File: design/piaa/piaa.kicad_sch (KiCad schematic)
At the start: 92 parts, among them J1 Screw_Terminal_01x03, J2 Conn_02x04_Counter_Clockwise, J3 Conn_02x01, J4 Conn_02x01, J5 Conn_02x01, J6 Screw_Terminal_01x06, J7 Screw_Terminal_01x05, P1 PS2805-4, Q1 FQT13N06L, Q2 FQT13N06L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

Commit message: fix symbols, begin layout
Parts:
- U8: footprint RPi_Pico:RPi_Pico_SMD_TH -> MCU_RaspberryPi_and_Boards:RPi_Pico_SMD_TH
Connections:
- net DIN2: now also P1.12 (C2); no longer P1.C2 (12)
- net DOUT4: no longer U4.3 (IN)
- net DOUT5: now also U4.3 (IN)
- net GND: now also Q1.3 (S), Q2.3 (S), Q3.3 (S), Q4.3 (S), Q5.3 (S), Q6.3 (S); no longer Q1.2 (S), Q2.2 (S), Q3.2 (S), Q4.2 (S), Q5.2 (S), Q6.2 (S)
- net at F3.2: now also Q3.4 (D); no longer Q3.3 (D)
- net at F2.2: now also Q2.4 (D); no longer Q2.3 (D)
- net at F1.2: now also Q1.4 (D); no longer Q1.3 (D)
- net at F6.2: now also Q6.4 (D); no longer Q6.3 (D)
- net at F4.2: now also Q4.4 (D); no longer Q4.3 (D)
- net at F5.2: now also Q5.4 (D); no longer Q5.3 (D)
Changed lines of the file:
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@@
     (effects (font (size 1.27 1.27)) (justify right))
   )
-  (hierarchical_label "DOUT4" (shape input) (at 25.4 180.34 180)
+  (hierarchical_label "DOUT5" (shape input) (at 25.4 180.34 180)
     (effects (font (size 1.27 1.27)) (justify right))
   )
@@
     (pin "2")
   )
-  (symbol (lib_id "piaalib:FQT13N06L") (at 58.42 121.92 0) (unit 1)
+  (symbol (lib_name "FQT13N06L_5") (lib_id "piaalib:FQT13N06L") (at 58.42 121.92 0) (unit 1)
     (in_bom yes) (on_board yes) (fields_autoplaced)
     (property "Reference" "Q2" (id 0) (at 64.77 120.6499 0)
@@
     (pin "2")
     (pin "3")
+    (pin "4")
   )
   (symbol (lib_id "power:GND") (at 63.5 191.77 0) (unit 1)
@@
     (pin "2")
     (pin "3")
+    (pin "4")
   )
   (symbol (lib_id "power:+5V") (at 151.13 104.14 0) (unit 1)
@@
     (property "Reference" "U8" (id 0) (at 147.32 13.97 0))
     (property "Value" "Pico" (id 1) (at 147.32 16.51 0))
-    (property "Footprint" "RPi_Pico:RPi_Pico_SMD_TH" (id 2) (at 147.32 45.72 90))
+    (property "Footprint" "MCU_RaspberryPi_and_Boards:RPi_Pico_SMD_TH" (id 2) (at 147.32 45.72 90))
     (property "Datasheet" "" (id 3) (at 147.32 45.72 0)
       (effects (font (size 1.27 1.27)) hide)
@@
     (pin "5")
   )
-  (symbol (lib_name "PTS12066V100_4") (lib_id "piaalib:PTS12066V100") (at 71.12 55.626 270) (unit 1)
+  (symbol (lib_id "piaalib:PTS12066V100") (at 71.12 55.626 270) (unit 1)
     (in_bom yes) (on_board yes)
     (property "Reference" "F6" (id 0) (at 66.04 58.42 90))
@@
     (pin "1")
   )
-  (symbol (lib_id "piaalib:FQT13N06L") (at 59.69 63.5 0) (unit 1)
+  (symbol (lib_name "FQT13N06L_3") (lib_id "piaalib:FQT13N06L") (at 59.69 63.5 0) (unit 1)
     (in_bom yes) (on_board yes) (fields_autoplaced)
     (property "Reference" "Q6" (id 0) (at 66.04 62.2299 0)
@@
     (pin "2")
     (pin "3")
+    (pin "4")
   )
   (symbol (lib_id "power:+5V") (at 21.59 166.37 0) (unit 1)
@@
     (pin "3")
   )
-  (symbol (lib_id "piaalib:FQT13N06L") (at 58.42 179.07 0) (unit 1)
+  (symbol (lib_name "FQT13N06L_4") (lib_id "piaalib:FQT13N06L") (at 58.42 179.07 0) (unit 1)
     (in_bom yes) (on_board yes) (fields_autoplaced)
     (property "Reference" "Q4" (id 0) (at 64.77 177.7999 0)
@@
     (pin "2")
     (pin "3")
+    (pin "4")
   )
   (symbol (lib_id "power:GND") (at 16.51 87.63 0) (unit 1)
@@
     (pin "2")
   )
-  (symbol (lib_name "PTS12066V100_3") (lib_id "piaalib:PTS12066V100") (at 71.12 25.146 270) (unit 1)
+  (symbol (lib_id "piaalib:PTS12066V100") (at 71.12 25.146 270) (unit 1)
     (in_bom yes) (on_board yes)
     (property "Reference" "F5" (id 0) (at 66.04 27.94 90))
@@
     (pin "2")
   )
-  (symbol (lib_name "PSD12C_1") (lib_id "piaalib:PSD12C") (at 175.26 142.24 270) (unit 1)
+  (symbol (lib_id "piaalib:PSD12C") (at 175.26 142.24 270) (unit 1)
     (in_bom yes) (on_board yes) (fields_autoplaced)
     (property "Reference" "D9" (id 0) (at 173.99 140.9699 90)
@@
     (pin "2")
   )
-  (symbol (lib_name "PTS12066V100_1") (lib_id "piaalib:PTS12066V100") (at 69.85 84.836 270) (unit 1)
+  (symbol (lib_id "piaalib:PTS12066V100") (at 69.85 84.836 270) (unit 1)
     (in_bom yes) (on_board yes)
     (property "Reference" "F1" (id 0) (at 64.77 87.63 90))
@@
     (pin "1")
   )
-  (symbol (lib_id "piaalib:FQT13N06L") (at 59.69 33.02 0) (unit 1)
+  (symbol (lib_name "FQT13N06L_2") (lib_id "piaalib:FQT13N06L") (at 59.69 33.02 0) (unit 1)
     (in_bom yes) (on_board yes) (fields_autoplaced)
     (property "Reference" "Q5" (id 0) (at 66.04 31.7499 0)
@@
     (pin "2")
     (pin "3")
+    (pin "4")
   )
   (symbol (lib_id "power:GND") (at 36.83 100.33 0) (unit 1)
@@
     (pin "10")
     (pin "11")
+    (pin "12")
     (pin "13")
     (pin "14")
@@
     (pin "8")
     (pin "9")
-    (pin "C2")
   )
   (symbol (lib_id "Device:R") (at 255.27 22.86 90) (unit 1)
@@
     (pin "2")
   )
-  (symbol (lib_id "piaalib:FQT13N06L") (at 58.42 149.86 0) (unit 1)
+  (symbol (lib_name "FQT13N06L_1") (lib_id "piaalib:FQT13N06L") (at 58.42 149.86 0) (unit 1)
     (in_bom yes) (on_board yes) (fields_autoplaced)
     (property "Reference" "Q3" (id 0) (at 64.77 148.5899 0)
@@
     (pin "2")
     (pin "3")
+    (pin "4")
   )
   (symbol (lib_id "power:GND") (at 16.51 175.26 0) (unit 1)
@@
     (pin "1")
   )
-  (symbol (lib_name "USMF020_1") (lib_id "piaalib:USMF020") (at 180.34 110.49 0) (unit 1)
+  (symbol (lib_id "piaalib:USMF020") (at 180.34 110.49 0) (unit 1)
     (in_bom yes) (on_board yes)
     (property "Reference" "PS1" (id 0) (at 181.61 111.76 0))
@@
     (pin "2")
   )
-  (symbol (lib_name "PTS12066V100_2") (lib_id "piaalib:PTS12066V100") (at 69.85 172.466 270) (unit 1)
+  (symbol (lib_id "piaalib:PTS12066V100") (at 69.85 172.466 270) (unit 1)
     (in_bom yes) (on_board yes)
     (property "Reference" "F4" (id 0) (at 64.77 175.26 90))
@@
     (pin "1")
   )
-  (symbol (lib_name "PTS12066V100_5") (lib_id "piaalib:PTS12066V100") (at 69.85 114.046 270) (unit 1)
+  (symbol (lib_id "piaalib:PTS12066V100") (at 69.85 114.046 270) (unit 1)
     (in_bom yes) (on_board yes)
     (property "Reference" "F2" (id 0) (at 64.77 116.84 90))
@@
     (pin "2")
   )
-  (symbol (lib_name "PSD12C_2") (lib_id "piaalib:PSD12C") (at 175.26 123.19 270) (unit 1)
+  (symbol (lib_id "piaalib:PSD12C") (at 175.26 123.19 270) (unit 1)
     (in_bom yes) (on_board yes)
     (property "Reference" "D8" (id 0) (at 173.99 120.65 90)
@@
     )
     (path "/28ea4dcd-d9fa-4361-9269-bd436148a234"
-      (reference "U8") (unit 1) (value "Pico") (footprint "RPi_Pico:RPi_Pico_SMD_TH")
+      (reference "U8") (unit 1) (value "Pico") (footprint "MCU_RaspberryPi_and_Boards:RPi_Pico_SMD_TH")
     )
     (path "/19057f4d-07e4-4313-ba58-58576df1fe00/c116edb4-51d5-471f-97e9-f783ce1a4554"

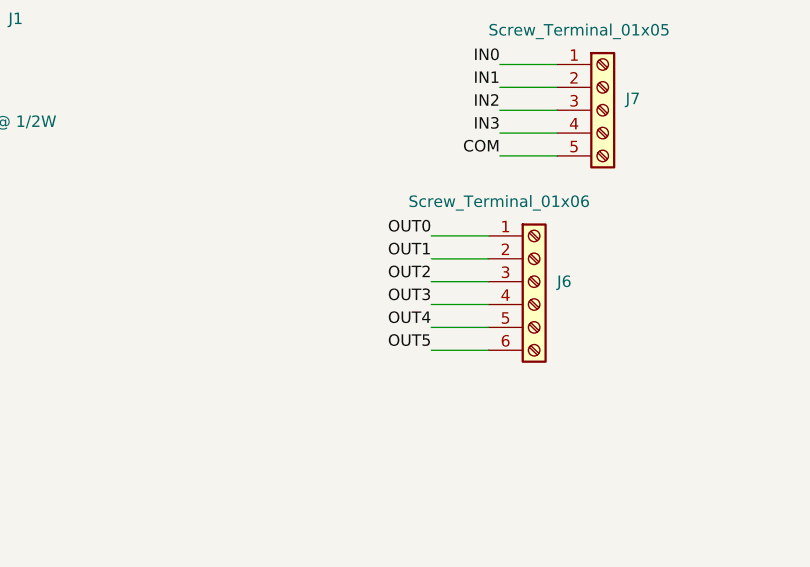
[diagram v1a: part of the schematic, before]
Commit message: update to pcb drawing
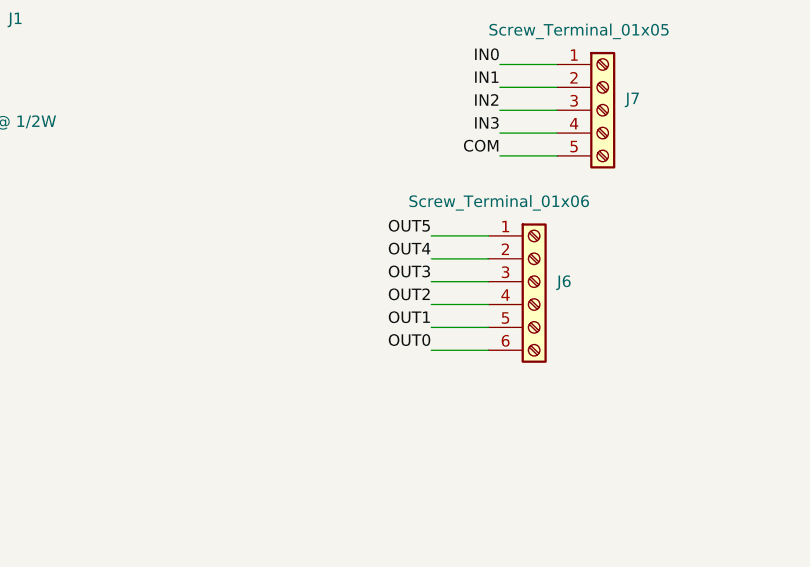
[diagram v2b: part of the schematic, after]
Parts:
- J7: footprint Connector_PinHeader_2.00mm:PinHeader_1x05_P2.00mm_Horizontal -> Connector_PinHeader_2.00mm:PinHeader_1x05_P2.00mm_Vertical
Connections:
- net OUT0: now also J6.6 (Pin_6); no longer J6.1 (Pin_1)
- net OUT1: now also J6.5 (Pin_5); no longer J6.2 (Pin_2)
- net OUT2: now also J6.4 (Pin_4); no longer J6.3 (Pin_3)
- net OUT3: now also J6.3 (Pin_3); no longer J6.4 (Pin_4)
- net OUT4: now also J6.2 (Pin_2); no longer J6.5 (Pin_5)
- net OUT5: now also J6.1 (Pin_1); no longer J6.6 (Pin_6)
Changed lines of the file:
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@@
     (effects (font (size 1.27 1.27)) (justify left bottom))
   )
-  (label "OUT5" (at 255.27 156.21 180)
+  (label "OUT0" (at 255.27 156.21 180)
     (effects (font (size 1.27 1.27)) (justify right bottom))
   )
@@
     (effects (font (size 1.27 1.27)) (justify left bottom))
   )
-  (label "OUT2" (at 255.27 148.59 180)
+  (label "OUT3" (at 255.27 148.59 180)
     (effects (font (size 1.27 1.27)) (justify right bottom))
   )
@@
     (effects (font (size 1.27 1.27)) (justify left bottom))
   )
-  (label "OUT1" (at 255.27 146.05 180)
+  (label "OUT4" (at 255.27 146.05 180)
     (effects (font (size 1.27 1.27)) (justify right bottom))
   )
@@
     (effects (font (size 1.27 1.27)) (justify left bottom))
   )
-  (label "OUT3" (at 255.27 151.13 180)
+  (label "OUT2" (at 255.27 151.13 180)
     (effects (font (size 1.27 1.27)) (justify right bottom))
   )
-  (label "OUT4" (at 255.27 153.67 180)
+  (label "OUT1" (at 255.27 153.67 180)
     (effects (font (size 1.27 1.27)) (justify right bottom))
   )
@@
     (effects (font (size 1.27 1.27)) (justify left bottom))
   )
-  (label "OUT0" (at 255.27 143.51 180)
+  (label "OUT5" (at 255.27 143.51 180)
     (effects (font (size 1.27 1.27)) (justify right bottom))
   )
@@
     (pin "2")
   )
-  (symbol (lib_name "FQT13N06L_5") (lib_id "piaalib:FQT13N06L") (at 58.42 121.92 0) (unit 1)
+  (symbol (lib_id "piaalib:FQT13N06L") (at 58.42 121.92 0) (unit 1)
     (in_bom yes) (on_board yes) (fields_autoplaced)
     (property "Reference" "Q2" (id 0) (at 64.77 120.6499 0)
@@
     (pin "1")
   )
-  (symbol (lib_name "FQT13N06L_3") (lib_id "piaalib:FQT13N06L") (at 59.69 63.5 0) (unit 1)
+  (symbol (lib_id "piaalib:FQT13N06L") (at 59.69 63.5 0) (unit 1)
     (in_bom yes) (on_board yes) (fields_autoplaced)
     (property "Reference" "Q6" (id 0) (at 66.04 62.2299 0)
@@
     (pin "3")
   )
-  (symbol (lib_name "FQT13N06L_4") (lib_id "piaalib:FQT13N06L") (at 58.42 179.07 0) (unit 1)
+  (symbol (lib_id "piaalib:FQT13N06L") (at 58.42 179.07 0) (unit 1)
     (in_bom yes) (on_board yes) (fields_autoplaced)
     (property "Reference" "Q4" (id 0) (at 64.77 177.7999 0)
@@
     (pin "1")
   )
-  (symbol (lib_name "FQT13N06L_2") (lib_id "piaalib:FQT13N06L") (at 59.69 33.02 0) (unit 1)
+  (symbol (lib_id "piaalib:FQT13N06L") (at 59.69 33.02 0) (unit 1)
     (in_bom yes) (on_board yes) (fields_autoplaced)
     (property "Reference" "Q5" (id 0) (at 66.04 31.7499 0)
@@
       (effects (font (size 1.27 1.27)) (justify left))
     )
-    (property "Footprint" "Connector_PinHeader_2.00mm:PinHeader_1x05_P2.00mm_Horizontal" (id 2) (at 274.32 129.54 0)
+    (property "Footprint" "Connector_PinHeader_2.00mm:PinHeader_1x05_P2.00mm_Vertical" (id 2) (at 274.32 129.54 0)
       (effects (font (size 1.27 1.27)) hide)
     )
@@
     (pin "2")
   )
-  (symbol (lib_name "FQT13N06L_1") (lib_id "piaalib:FQT13N06L") (at 58.42 149.86 0) (unit 1)
+  (symbol (lib_id "piaalib:FQT13N06L") (at 58.42 149.86 0) (unit 1)
     (in_bom yes) (on_board yes) (fields_autoplaced)
     (property "Reference" "Q3" (id 0) (at 64.77 148.5899 0)
@@
     )
     (path "/ba496337-43f2-4662-a8b9-201654f85c6e"
-      (reference "J7") (unit 1) (value "Screw_Terminal_01x05") (footprint "Connector_PinHeader_2.00mm:PinHeader_1x05_P2.00mm_Horizontal")
+      (reference "J7") (unit 1) (value "Screw_Terminal_01x05") (footprint "Connector_PinHeader_2.00mm:PinHeader_1x05_P2.00mm_Vertical")
     )
     (path "/19057f4d-07e4-4313-ba58-58576df1fe00/4fc6b216-318e-4955-9b3e-ba0aeac990a8"
-      (reference "J8") (unit 1) (value "Screw_Terminal_01x02") (footprint "Connector_PinHeader_2.00mm:PinHeader_1x02_P2.00mm_Horizontal")
+      (reference "J8") (unit 1) (value "Screw_Terminal_01x02") (footprint "Connector_PinHeader_2.00mm:PinHeader_1x02_P2.00mm_Vertical")
     )
     (path "/d4502304-4ea1-4353-9792-077ebe9f4ce6"

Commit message: updates to schematic
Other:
- company: (none) -> Patricio Whittingslow
- title: (none) -> PIAA
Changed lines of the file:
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@@
 (kicad_sch (version 20211123) (generator eeschema)
   (paper "A4")
+  (title_block
+    (title "PIAA")
+    (date "5 March 2023")
+    (rev "A.0")
+    (company "Patricio Whittingslow")
+  )
   (junction (at 25.4 109.22) (diameter 0) (color 0 0 0 0)
   )

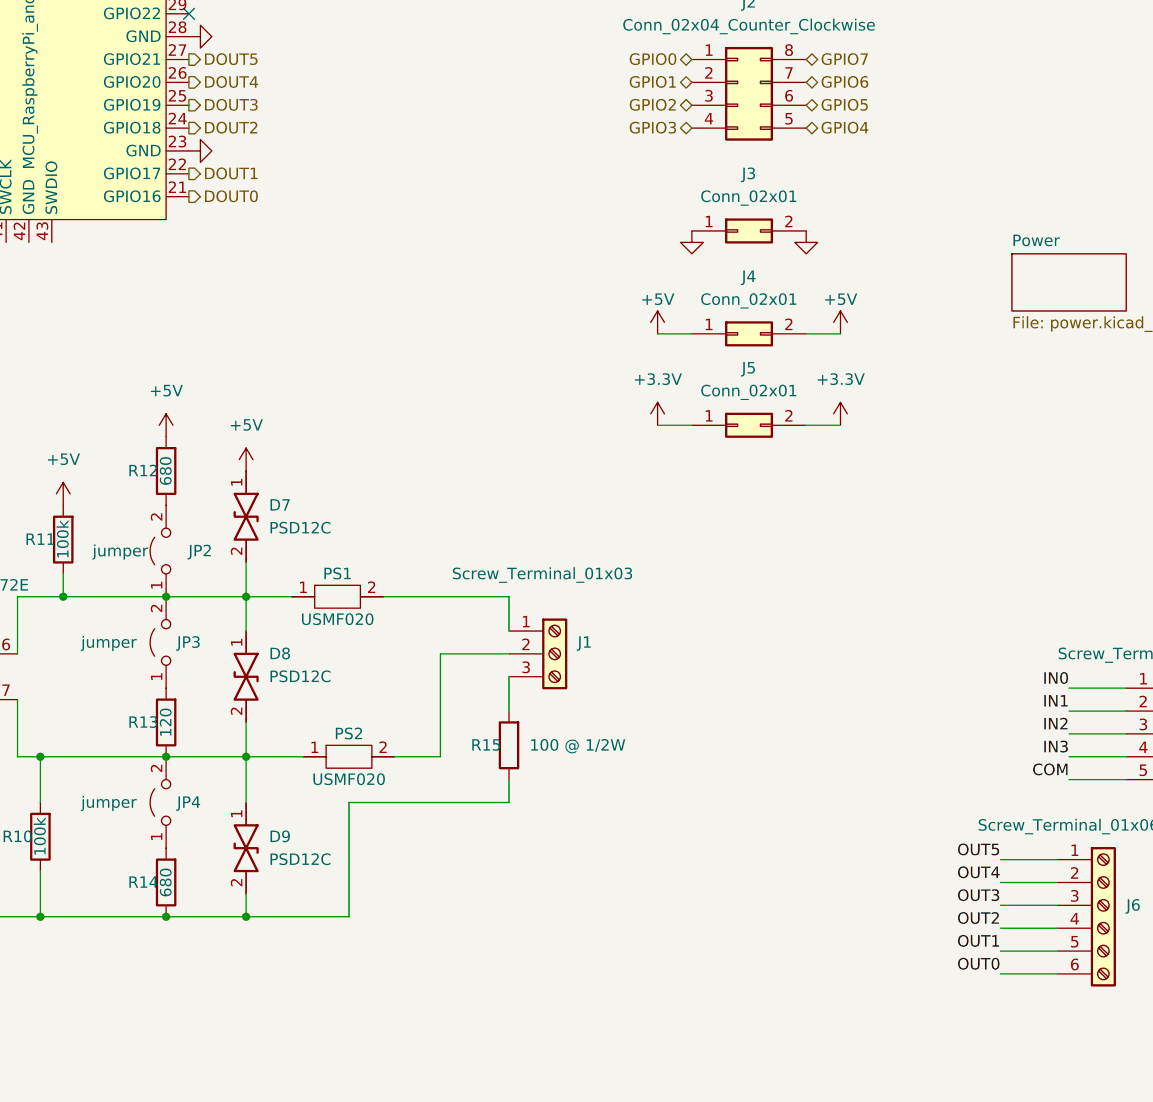
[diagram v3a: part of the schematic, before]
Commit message: fix header and bornier size
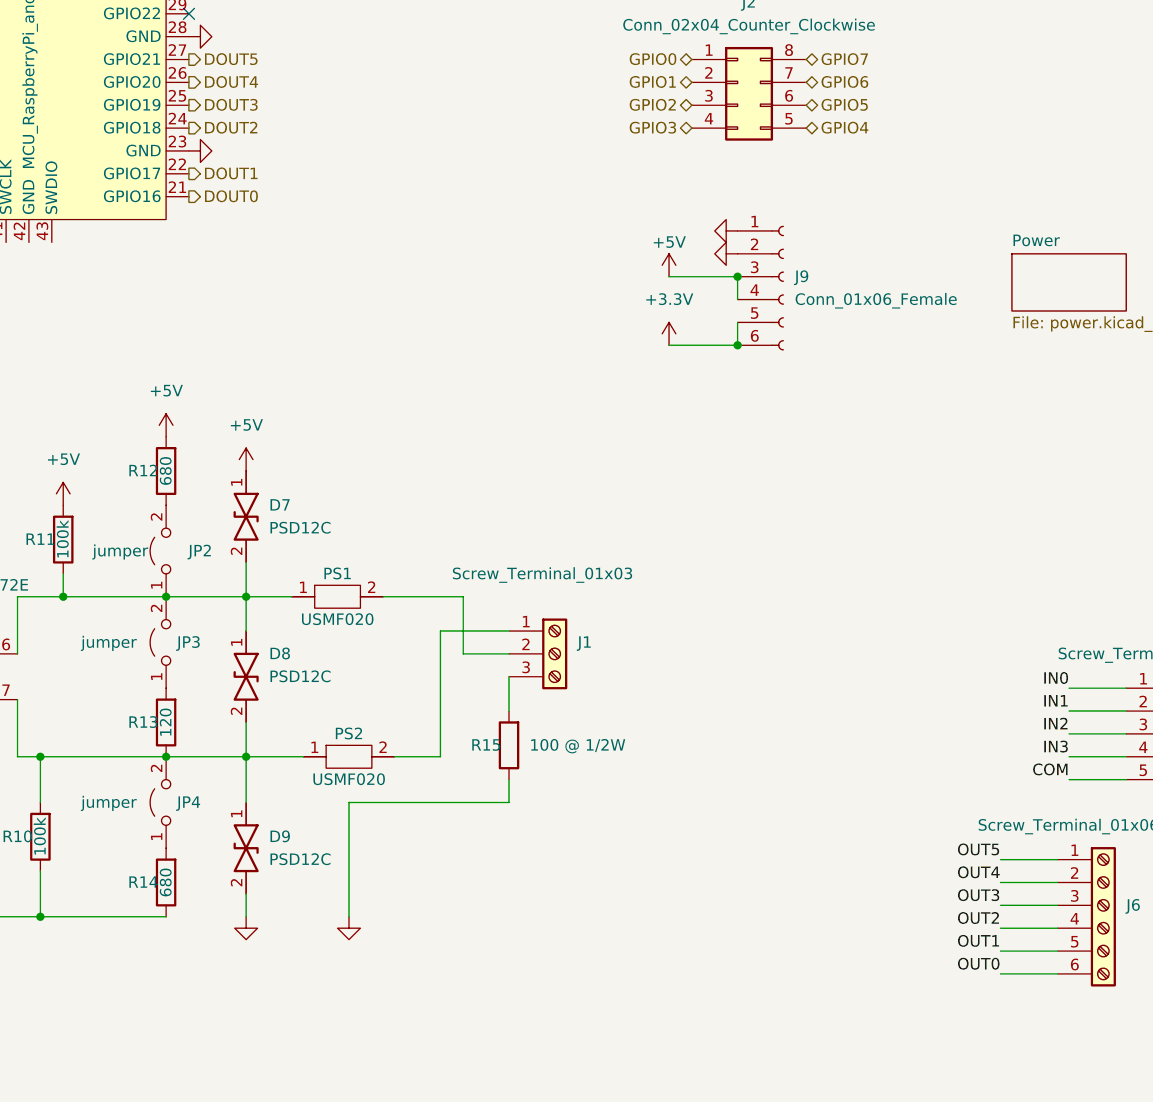
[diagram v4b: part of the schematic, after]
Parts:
- removed J3, J4, J5: Conn_02x01, Connector_PinHeader_1.27mm:PinHeader_1x02_P1.27mm_Vertical, symbol Connector_Generic:Conn_02x01
- added J9: Conn_01x06_Female, Connector_PinHeader_2.54mm:PinHeader_2x03_P2.54mm_Vertical, symbol Connector:Conn_01x06_Female
- J1: footprint Connector_PinHeader_2.00mm:PinHeader_1x03_P2.00mm_Vertical -> TerminalBlock:TerminalBlock_bornier-3_P5.08mm
- J2: footprint Connector_PinHeader_1.27mm:PinHeader_2x04_P1.27mm_Vertical -> Connector_PinHeader_2.54mm:PinHeader_2x04_P2.54mm_Vertical
- J6: footprint Connector_PinHeader_2.00mm:PinHeader_1x06_P2.00mm_Horizontal -> TerminalBlock:TerminalBlock_bornier-6_P5.08mm
- J7: footprint Connector_PinHeader_2.00mm:PinHeader_1x05_P2.00mm_Vertical -> TerminalBlock:TerminalBlock_bornier-5_P5.08mm
- JP1, JP2, JP3, JP4: footprint Connector_PinHeader_1.27mm:PinHeader_1x02_P1.27mm_Vertical -> Connector_PinHeader_2.54mm:PinHeader_1x02_P2.54mm_Vertical
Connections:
- net +3V3: now also J9.5 (Pin_5), J9.6 (Pin_6)
- net +5V: now also J9.3 (Pin_3), J9.4 (Pin_4)
- net GND: now also J9.1 (Pin_1), J9.2 (Pin_2)
- net at PS2.2: now also J1.1 (Pin_1); no longer J1.2 (Pin_2)
- net at PS1.2: now also J1.2 (Pin_2); no longer J1.1 (Pin_1)
